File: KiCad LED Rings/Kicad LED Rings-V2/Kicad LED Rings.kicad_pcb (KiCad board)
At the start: 4 copper layers, 30 x 30 mm, 28 parts, among them J1 Conn_01x02_Female, J2 Conn_01x02_Male, U1 LM3509SD_NOPB

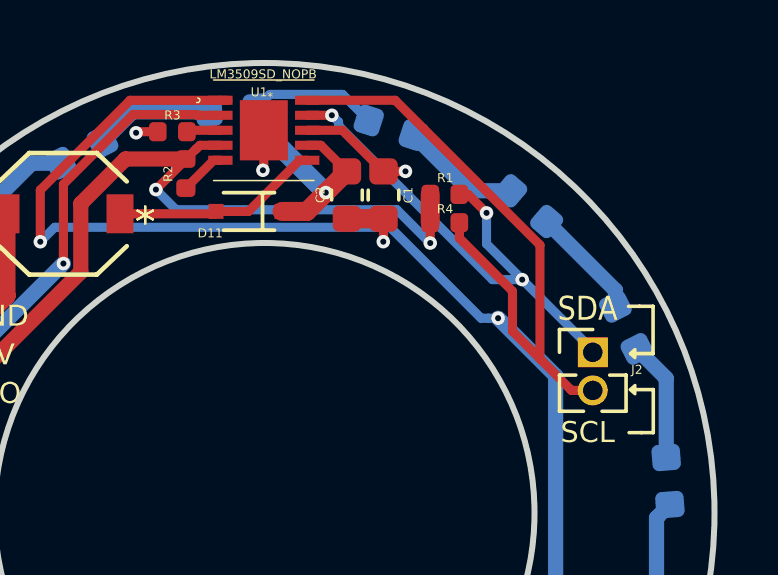
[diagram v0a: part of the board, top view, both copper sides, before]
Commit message: Updated LED Ring PCB
Changed '10uF 0603 25V' to '10uF 1210 50V'
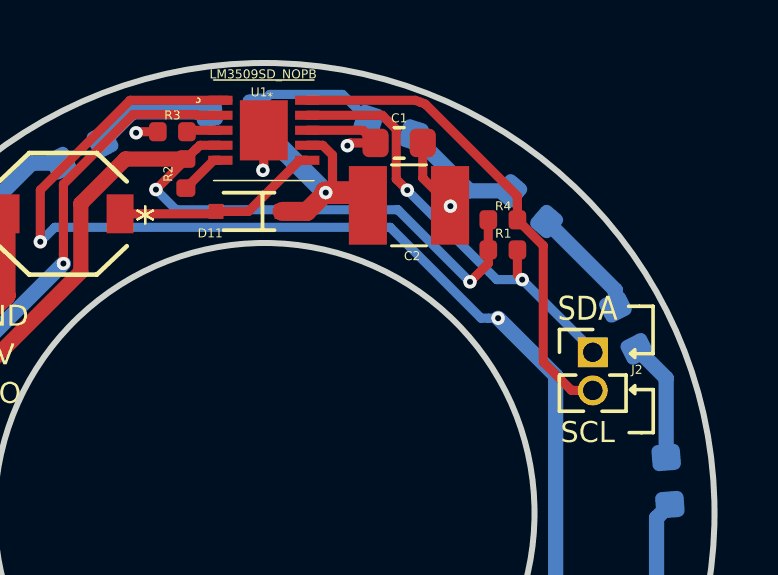
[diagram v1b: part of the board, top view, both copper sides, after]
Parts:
- removed G***: LOGO, .Logo:Minicam_LED_Ring
- C2: footprint .Capacitor_SMD:C_0603_1608Metric -> Capacitor:C_1210_3225Metric_L
- R1, R4: value 10K -> 3K
- R2: value 10K -> 9.5k
- R3: value 8K -> 9.5k
- moved R1 2.68 mm to (117.6, 71.1)
- moved C2 2.10 mm to (114.5, 69.7), turned to 180 degrees
- moved R4 1.94 mm to (117.6, 70.1)
- moved C1 1.81 mm to (114.1, 67.6), turned to 180 degrees
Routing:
- net SCL: track 21.4 -> 16.2 mm
- net +2V8: track 27.2 -> 29.7 mm
- net SDA: track 16.8 -> 14.9 mm, vias 3 -> 2
- net OVP: track 12.5 -> 13.7 mm

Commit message: Updated LED ring PCB
Added LED Ring PCB logo
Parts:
- added G***: LOGO, .Logo:Minicam_LED_Ring, B.Cu at (101.0, 80.1)

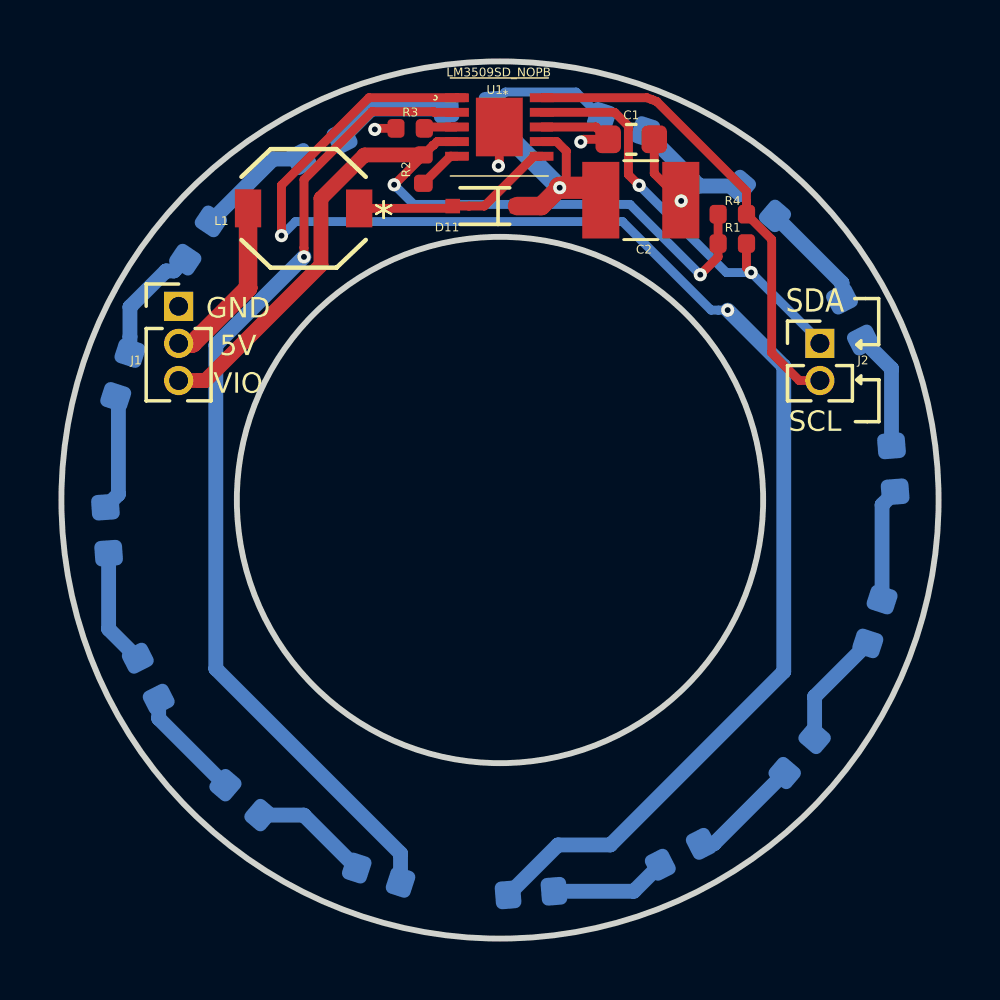
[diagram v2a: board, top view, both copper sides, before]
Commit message: Upldated LED ring PCB
Changed 10uF Cout to C2012X5R1E225M125AC;
Changed 10uH inductor to NRS4012T100MDGJ;
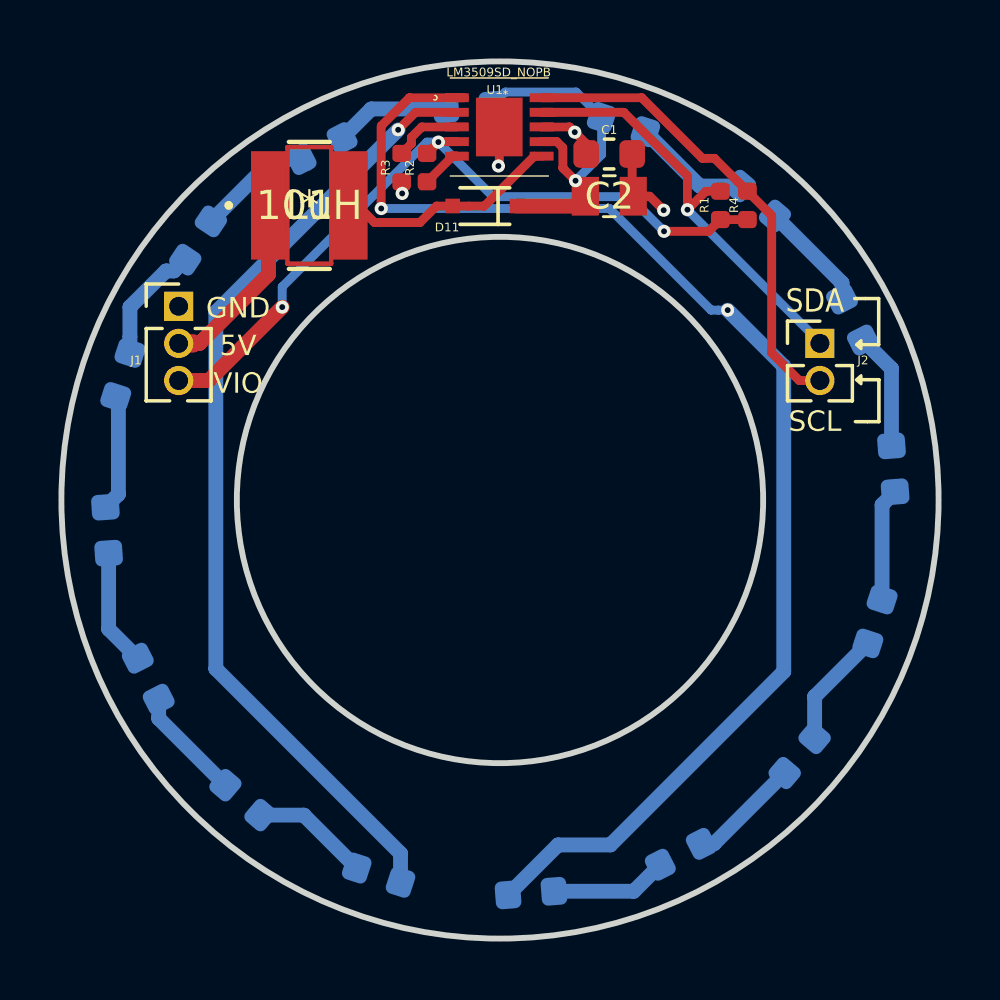
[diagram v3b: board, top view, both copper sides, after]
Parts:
- C2: value 10uF -> 2.2uF; footprint Capacitor:C_1210_3225Metric_L -> .Capacitor:C_0805_2012Metric_L
- L1: footprint footprints:VLF4012AT-100MR79 -> footprints:NRS4012T100MDGJ
- moved R3 1.37 mm to (106.3, 68.5), turned to 90 degrees
- moved R1 1.37 mm to (117.2, 69.8), turned to 270 degrees
- moved C2 1.09 mm to (113.4, 69.5)
- moved C1 0.91 mm to (113.4, 68.1)
- moved R4 0.60 mm to (118.1, 69.8), turned to 270 degrees
- moved L1 0.22 mm to (103.1, 69.8), turned to 0 degrees
- moved R2 0.14 mm to (107.2, 68.5)
- moved G*** 0.10 mm to (101.0, 80.2)
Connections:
- L1 pad 1: Net-(D11-Pad2) -> +5V
- L1 pad 2: +5V -> Net-(D11-Pad2)
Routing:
- net Net-(D2-Pad1): track 51.7 -> 45.1 mm
- net +2V8: track 29.7 -> 25.9 mm, vias 2 -> 3
- net OVP: track 13.7 -> 12.1 mm
- net Net-(R3-Pad2): track 1.14 -> 2.39 mm
- net Net-(D1-Pad1): track 34.1 -> 33.2 mm
- net SDA: track 14.9 -> 15.3 mm, vias 2 -> 1

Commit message: Updated LED ring PCB
Removed the vias off the pads
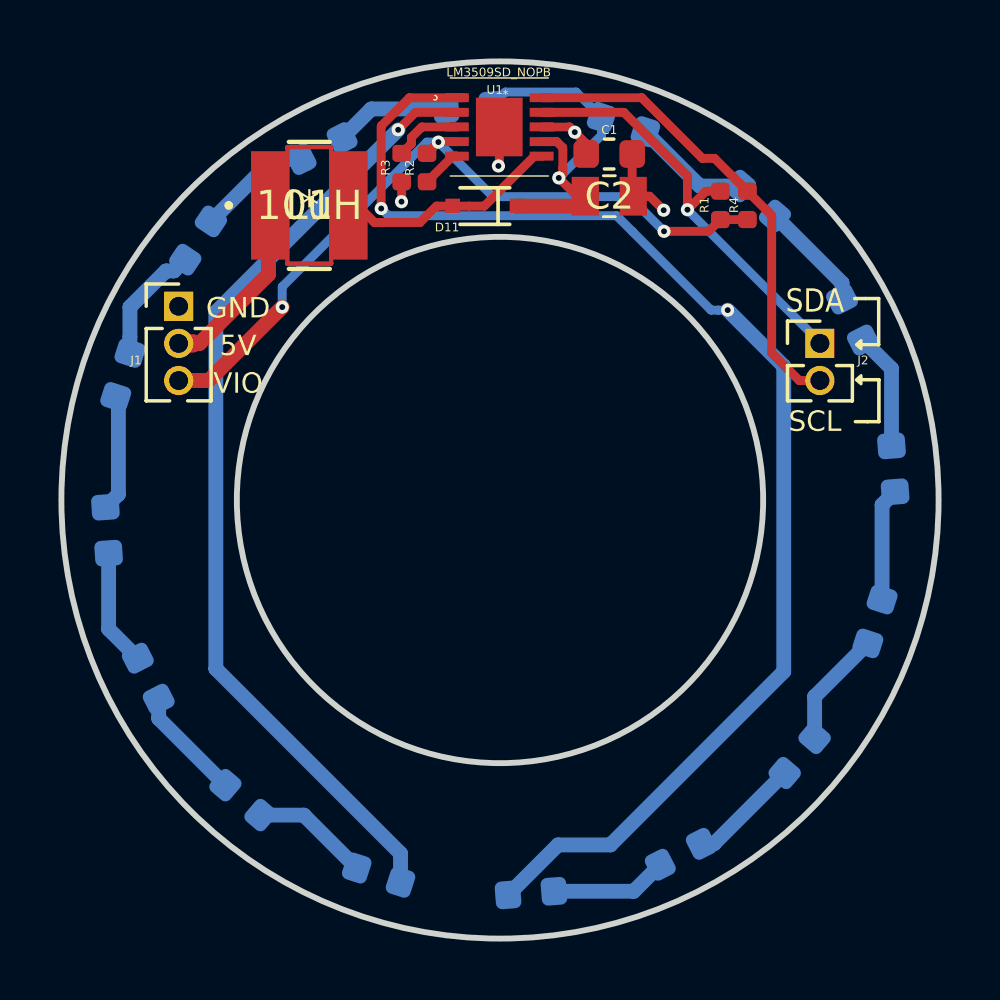
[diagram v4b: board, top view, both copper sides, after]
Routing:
- net OVP: track 12.1 -> 12.7 mm
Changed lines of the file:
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@@
     (thickness 1.6)
     (drawings 30)
-    (tracks 146)
+    (tracks 150)
     (zones 0)
     (modules 28)
@@
   (segment (start 109.6264 67.15252) (end 109.6264 68.45554) (width 0.3048) (layer F.Cu) (net 2))
   (segment (start 109.6264 68.45554) (end 109.59592 68.48602) (width 0.3048) (layer F.Cu) (net 2))
-  (via (at 106.30408 69.42582) (size 0.45) (drill 0.2) (layers F.Cu B.Cu) (net 2))
-  (segment (start 106.2863 69.0269) (end 106.2863 69.40804) (width 0.2032) (layer F.Cu) (net 2))
-  (segment (start 106.2863 69.40804) (end 106.30408 69.42582) (width 0.2032) (layer F.Cu) (net 2))
   (via (at 115.24742 69.99986) (size 0.45) (drill 0.2) (layers F.Cu B.Cu) (net 2))
   (segment (start 114.20814 69.5198) (end 114.76736 69.5198) (width 0.3048) (layer F.Cu) (net 2))
@@
   (segment (start 114.17066 69.48232) (end 114.20814 69.5198) (width 0.3048) (layer F.Cu) (net 2))
   (segment (start 114.17066 68.07708) (end 114.17066 69.48232) (width 0.3048) (layer F.Cu) (net 2))
+  (via (at 106.28122 69.70776) (size 0.45) (drill 0.2) (layers F.Cu B.Cu) (net 2))
+  (segment (start 106.2863 69.0269) (end 106.2863 69.70268) (width 0.3048) (layer F.Cu) (net 2))
+  (segment (start 106.2863 69.70268) (end 106.28122 69.70776) (width 0.3048) (layer F.Cu) (net 2))
   (segment (start 102.94004 90.68652) (end 104.750017 92.496497) (width 0.508) (layer B.Cu) (net 3))
   (segment (start 101.45714 90.68652) (end 102.94004 90.68652) (width 0.508) (layer B.Cu) (net 3))
@@
   (segment (start 117.118702 73.41616) (end 117.4369 73.41616) (width 0.3048) (layer B.Cu) (net 5))
   (segment (start 116.868202 73.41616) (end 117.118702 73.41616) (width 0.3048) (layer B.Cu) (net 5))
-  (segment (start 105.5878 69.94144) (end 113.393482 69.94144) (width 0.3048) (layer B.Cu) (net 5))
-  (segment (start 113.393482 69.94144) (end 116.868202 73.41616) (width 0.3048) (layer B.Cu) (net 5))
+  (segment (start 113.638803 70.186761) (end 114.180751 70.728709) (width 0.3048) (layer B.Cu) (net 5))
+  (segment (start 105.833121 70.186761) (end 113.638803 70.186761) (width 0.3048) (layer B.Cu) (net 5))
+  (segment (start 105.5878 69.94144) (end 105.833121 70.186761) (width 0.3048) (layer B.Cu) (net 5))
+  (segment (start 114.180751 70.728709) (end 116.868202 73.41616) (width 0.3048) (layer B.Cu) (net 5))
   (segment (start 96.265053 84.323263) (end 97.262302 85.320512) (width 0.508) (layer B.Cu) (net 6))
   (segment (start 96.265053 81.727762) (end 96.265053 84.323263) (width 0.508) (layer B.Cu) (net 6))
@@
   (segment (start 110.23364 69.85762) (end 112.23032 69.85762) (width 0.508) (layer F.Cu) (net 10))
   (segment (start 112.56814 69.3248) (end 112.56814 69.5198) (width 0.3048) (layer F.Cu) (net 10))
-  (segment (start 111.79834 68.555) (end 112.23363 68.99029) (width 0.3048) (layer F.Cu) (net 10))
   (segment (start 111.79834 67.860659) (end 111.79834 68.555) (width 0.3048) (layer F.Cu) (net 10))
   (segment (start 111.5902 67.652519) (end 111.79834 67.860659) (width 0.3048) (layer F.Cu) (net 10))
   (segment (start 111.0742 67.652519) (end 111.5902 67.652519) (width 0.3048) (layer F.Cu) (net 10))
-  (segment (start 112.23363 68.99029) (end 112.56814 69.3248) (width 0.3048) (layer F.Cu) (net 10))
-  (via (at 112.23363 68.99029) (size 0.45) (drill 0.2) (layers F.Cu B.Cu) (net 10))
-  (segment (start 113.124323 68.099597) (end 112.23363 68.99029) (width 0.3048) (layer B.Cu) (net 10))
-  (segment (start 113.124323 66.827889) (end 113.124323 68.099597) (width 0.3048) (layer B.Cu) (net 10))
+  (via (at 111.66094 68.89496) (size 0.45) (drill 0.2) (layers F.Cu B.Cu) (net 10))
+  (segment (start 111.79834 68.555) (end 111.79834 68.75756) (width 0.3048) (layer F.Cu) (net 10))
+  (segment (start 111.79834 68.75756) (end 111.66094 68.89496) (width 0.3048) (layer F.Cu) (net 10))
+  (segment (start 113.124323 67.431577) (end 111.66094 68.89496) (width 0.3048) (layer B.Cu) (net 10))
+  (segment (start 113.124323 66.827889) (end 113.124323 67.431577) (width 0.3048) (layer B.Cu) (net 10))
+  (segment (start 112.28578 69.5198) (end 111.66094 68.89496) (width 0.3048) (layer F.Cu) (net 10))
+  (segment (start 112.56814 69.5198) (end 112.28578 69.5198) (width 0.3048) (layer F.Cu) (net 10))
   (segment (start 108.58844 69.85762) (end 108.03364 69.85762) (width 0.3048) (layer F.Cu) (net 11))
   (segment (start 109.115101 69.85762) (end 108.58844 69.85762) (width 0.3048) (layer F.Cu) (net 11))
